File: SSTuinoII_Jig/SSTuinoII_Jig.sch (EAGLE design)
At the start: 13 parts, among them J1 MuseLab CMSIS-DAP, Q1 BS170

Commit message: finalised test jig
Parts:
- added S1: (no value), SparkFun-Switches:SWITCH-SPDT-PTH-11.6X4.0MM-KIT
- J1: value MuseLab CMSIS-DAP -> MuseLab CMSIS-DAP Only
- renumbered J2 to ESPTX_J, J3 to ESPRX_J
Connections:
- new net PWR: J1.10, S1.P
- net 5V: now also S1.O; no longer J1.10
- net GND: now also U$1.A25
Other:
- note added: "Pinout has been confirmed"
- moved on the sheet: ESP_IO0, ESP_RESET, POWER, R1

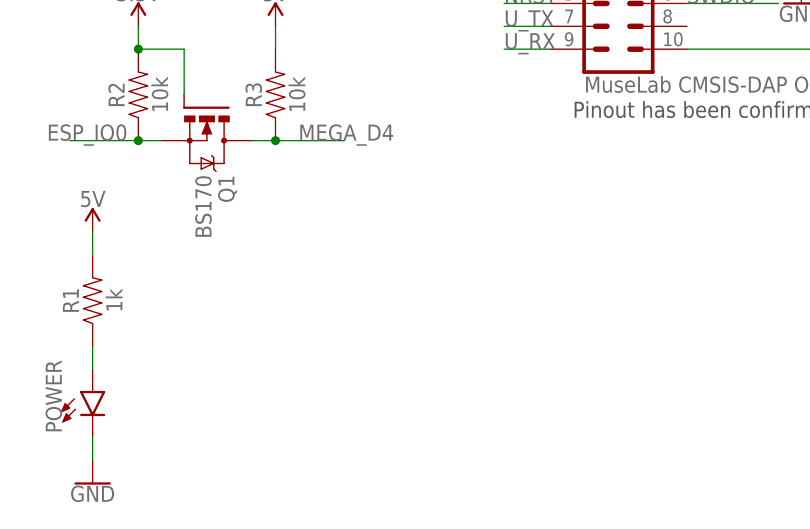
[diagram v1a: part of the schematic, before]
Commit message: final version of the revA jig, revB incoming soon
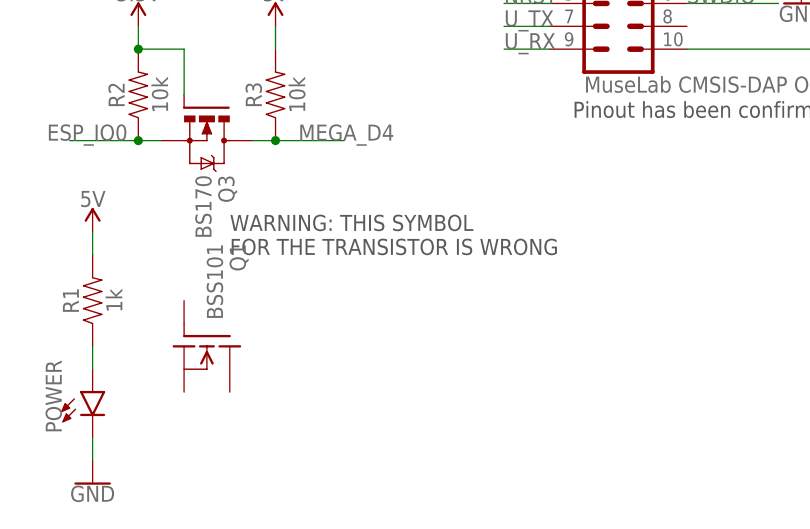
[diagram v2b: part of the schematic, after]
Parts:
- added Q3: BS170, Transistor:NMOSFET_BS170-TO92
- Q1: value BS170 -> BSS101; device Transistor:NMOSFET_BS170-TO92 -> transistor-fet:BSS101
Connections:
- net 3.3V: now also Q3.G; no longer Q1.G
- net ESP_IO0: now also Q3.S; no longer Q1.S
- net MEGA_D4: now also Q3.D; no longer Q1.D
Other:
- note added: "WARNING: THIS SYMBOL FOR THE TRANSISTOR IS WRONG"
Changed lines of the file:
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@@
 <part name="ESPRX_J" library="OPL_Connector" library_urn="urn:adsk.eagle:library:8004395" deviceset="DIP-BLACK-JUMPER" device="" package3d_urn="urn:adsk.eagle:package:8004540/1"/>
 <part name="LS1" library="SparkFun-Electromechanical" library_urn="urn:adsk.eagle:library:516" deviceset="BUZZER" device="-PTH_KIT" package3d_urn="urn:adsk.eagle:package:38556/1"/>
-<part name="Q1" library="Transistor" library_urn="urn:adsk.eagle:library:16378713" deviceset="NMOSFET_" device="-TO92" package3d_urn="urn:adsk.eagle:package:16378726/2" technology="BS170" value="BS170"/>
+<part name="Q3" library="Transistor" library_urn="urn:adsk.eagle:library:16378713" deviceset="NMOSFET_" device="-TO92" package3d_urn="urn:adsk.eagle:package:16378726/2" technology="BS170" value="BS170"/>
 <part name="R2" library="SparkFun-Resistors" library_urn="urn:adsk.eagle:library:532" deviceset="10KOHM" device="-HORIZ_KIT-1/4W-1%" package3d_urn="urn:adsk.eagle:package:39661/1" value="10k"/>
 <part name="R3" library="SparkFun-Resistors" library_urn="urn:adsk.eagle:library:532" deviceset="10KOHM" device="-HORIZ_KIT-1/4W-1%" package3d_urn="urn:adsk.eagle:package:39661/1" value="10k"/>
@@
 <part name="S1" library="SparkFun-Switches" library_urn="urn:adsk.eagle:library:535" deviceset="SWITCH-SPDT" device="-PTH-11.6X4.0MM-KIT" package3d_urn="urn:adsk.eagle:package:40178/1"/>
 <part name="GND7" library="SparkFun-PowerSymbols" library_urn="urn:adsk.eagle:library:530" deviceset="GND" device=""/>
+<part name="Q1" library="transistor-fet" library_urn="urn:adsk.eagle:library:396" deviceset="BSS101" device="" package3d_urn="urn:adsk.eagle:package:28523/2"/>
 </parts>
 <sheets>
@@
 <text x="81.28" y="154.94" size="1.778" layer="97">NC</text>
 <text x="104.14" y="83.82" size="1.778" layer="97">Pinout has been confirmed</text>
+<text x="66.04" y="68.58" size="1.778" layer="97">WARNING: THIS SYMBOL
+FOR THE TRANSISTOR IS WRONG</text>
 </plain>
 <instances>
@@
 <attribute name="NAME" x="71.12" y="114.046" size="1.778" layer="95" font="vector"/>
 </instance>
-<instance part="Q1" gate="G$1" x="63.5" y="83.82" smashed="yes" rot="R270">
+<instance part="Q3" gate="G$1" x="63.5" y="83.82" smashed="yes" rot="R270">
 <attribute name="NAME" x="64.77" y="77.47" size="1.778" layer="95" rot="R270"/>
 <attribute name="VALUE" x="62.23" y="77.47" size="1.778" layer="96" rot="R270"/>
@@
 <instance part="GND7" gate="1" x="55.88" y="124.46" smashed="yes">
 <attribute name="VALUE" x="55.88" y="124.206" size="1.778" layer="96" align="top-center"/>
+</instance>
+<instance part="Q1" gate="G$1" x="63.5" y="58.42" smashed="yes" rot="R270">
+<attribute name="VALUE" x="63.5" y="69.85" size="1.778" layer="96" rot="R270"/>
+<attribute name="NAME" x="66.04" y="69.85" size="1.778" layer="95" rot="R270"/>
 </instance>
 </instances>
@@
 </segment>
 <segment>
-<pinref part="Q1" gate="G$1" pin="G"/>
+<pinref part="Q3" gate="G$1" pin="G"/>
 <wire x1="60.96" y1="86.36" x2="60.96" y2="91.44" width="0.1524" layer="91"/>
 <pinref part="R2" gate="G$1" pin="2"/>
@@
 </segment>
 <segment>
-<pinref part="Q1" gate="G$1" pin="D"/>
+<pinref part="Q3" gate="G$1" pin="D"/>
 <pinref part="R3" gate="G$1" pin="1"/>
 <wire x1="68.58" y1="81.28" x2="71.12" y2="81.28" width="0.1524" layer="91"/>
@@
 </segment>
 <segment>
-<pinref part="Q1" gate="G$1" pin="S"/>
+<pinref part="Q3" gate="G$1" pin="S"/>
 <pinref part="R2" gate="G$1" pin="1"/>
 <wire x1="58.42" y1="81.28" x2="55.88" y2="81.28" width="0.1524" layer="91"/>
@@
 </drawing>
 <compatibility>
+<note version="6.3" minversion="6.2.2" severity="warning">
+Since Version 6.2.2 text objects can contain more than one line,
+which will not be processed correctly with this version.
+</note>
 <note version="8.2" severity="warning">
 Since Version 8.2, EAGLE supports online libraries. The ids

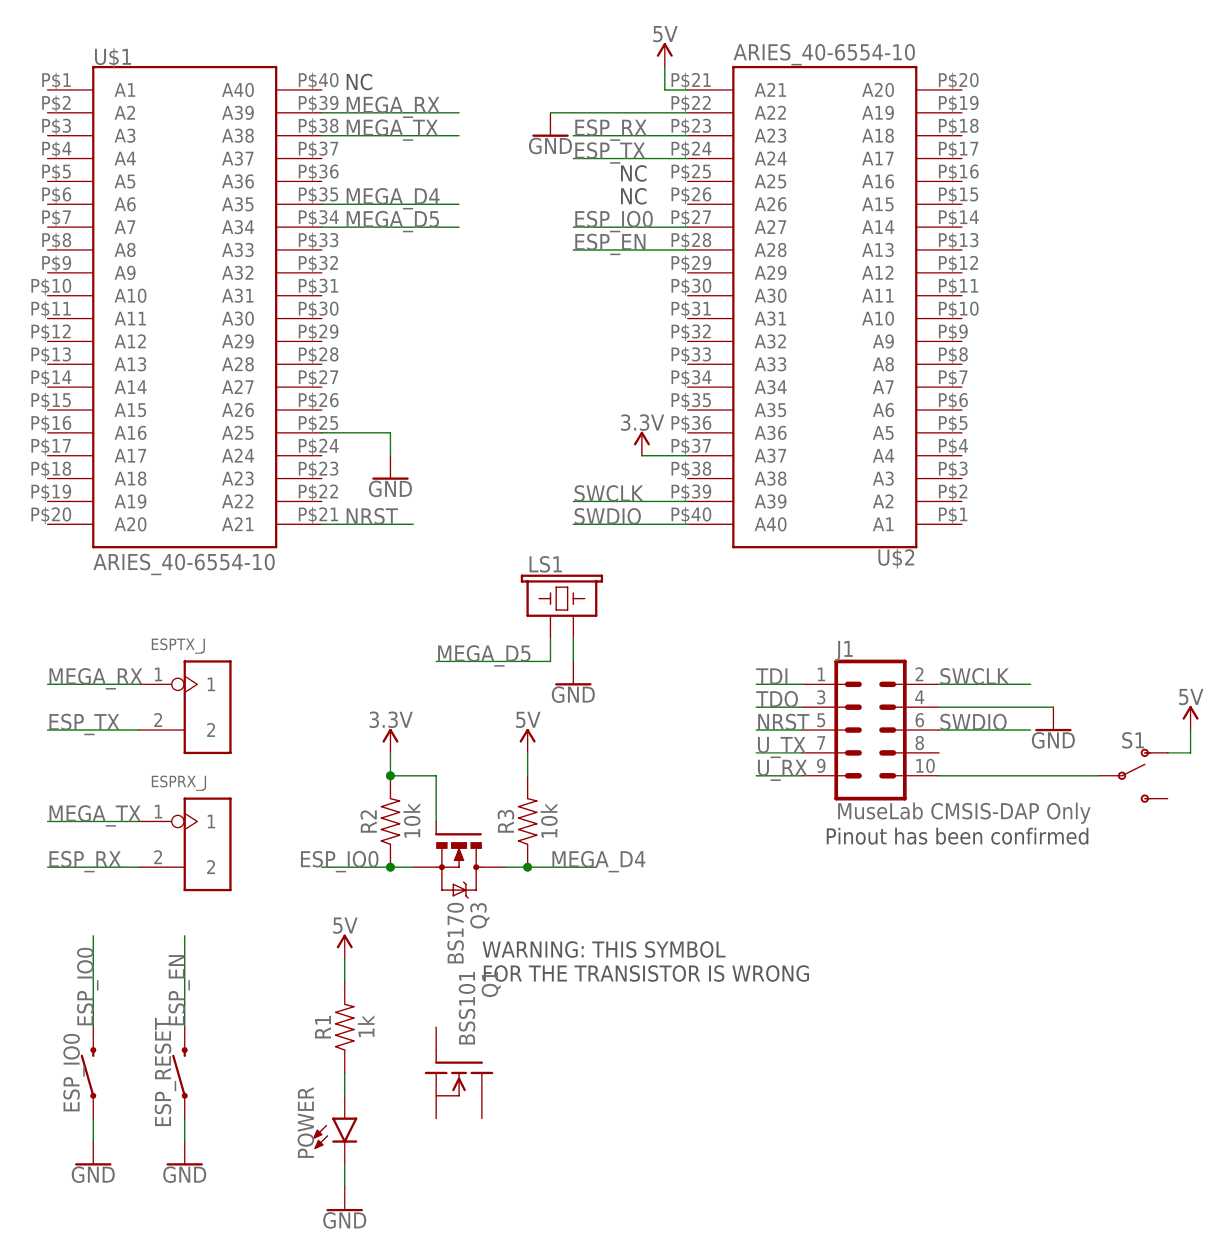
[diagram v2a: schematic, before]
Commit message: updated test jig
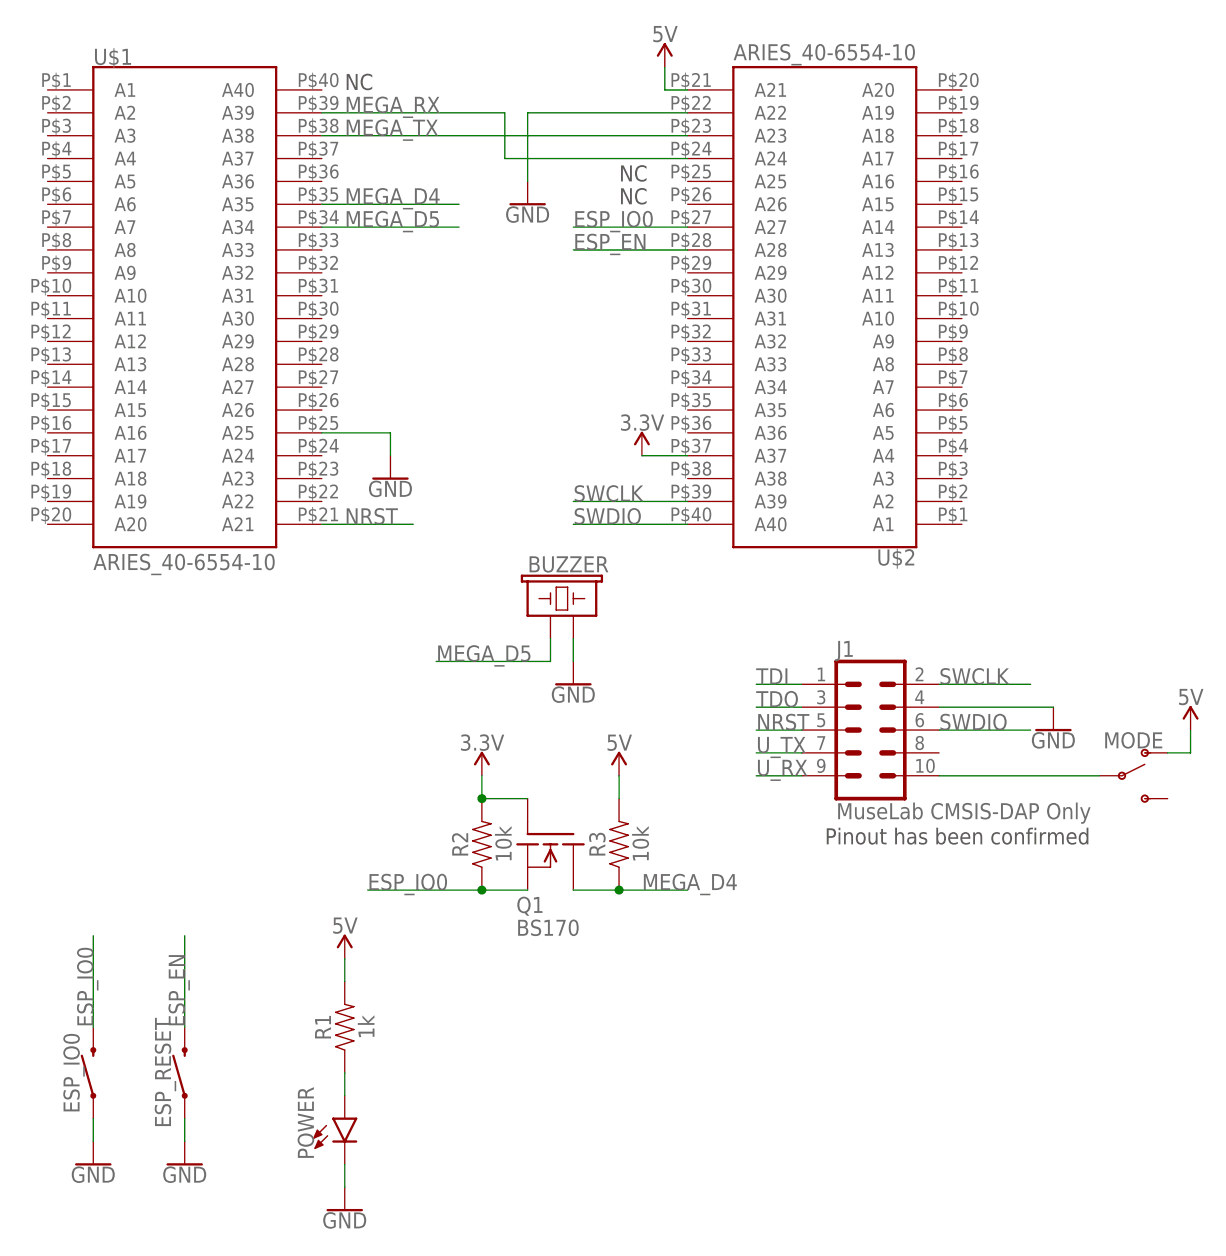
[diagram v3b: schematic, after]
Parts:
- removed ESPRX_J, ESPTX_J: (no value), OPL_Connector:DIP-BLACK-JUMPER
- removed Q3: BS170, Transistor:NMOSFET_BS170-TO92
- Q1: value BSS101 -> BS170
- renumbered LS1 to BUZZER, S1 to MODE
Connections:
- removed net ESP_RX: ESPRX_J.2, U$2.A23
- removed net ESP_TX: ESPTX_J.2, U$2.A24
- net 3.3V: now also Q1.G; no longer Q3.G
- net ESP_IO0: now also Q1.S; no longer Q3.S
- net MEGA_D4: now also Q1.D; no longer Q3.D
- net MEGA_RX: now also U$2.A24; no longer ESPTX_J.1
- net MEGA_TX: now also U$2.A23; no longer ESPRX_J.1
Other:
- note removed: "WARNING: THIS SYMBOL FOR THE TRANSISTOR IS WRONG"
- moved on the sheet: Q1, R2, R3
